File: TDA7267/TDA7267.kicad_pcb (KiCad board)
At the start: 2 copper layers, 43 x 39 mm, 18 parts, among them U1 TDA7267

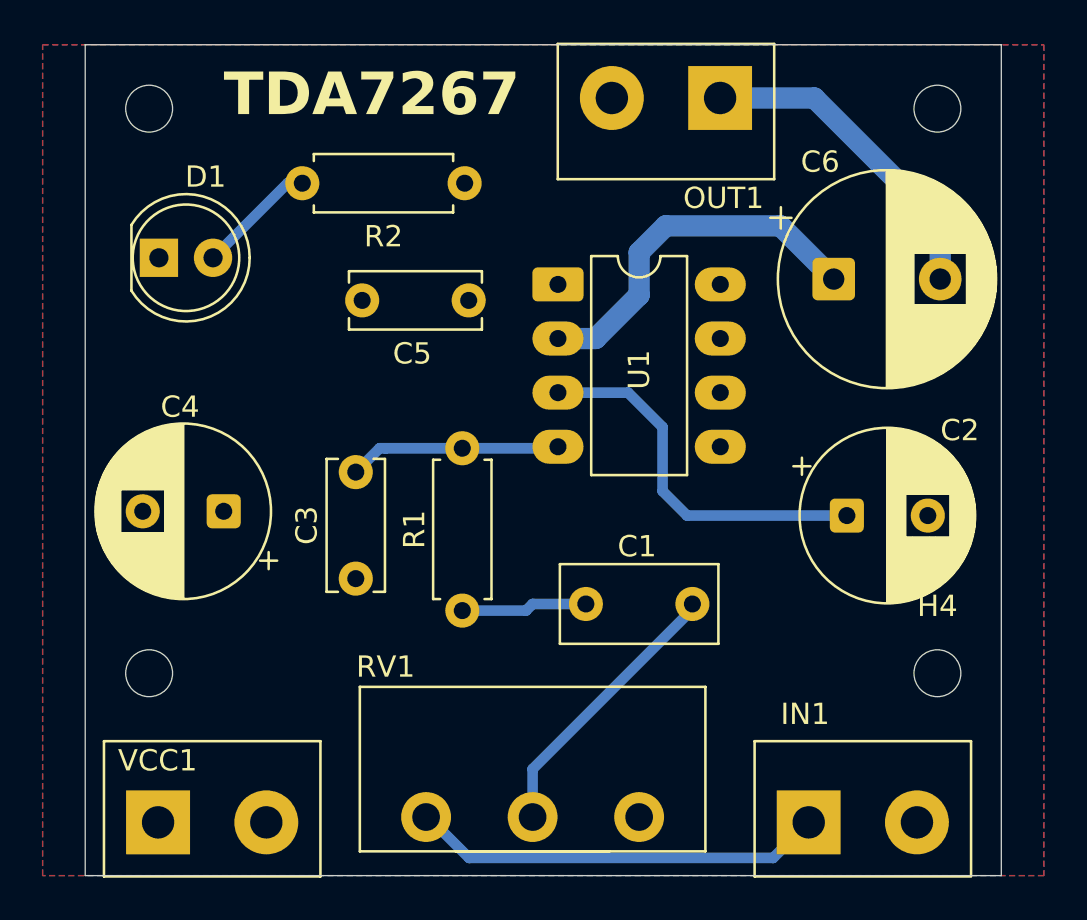
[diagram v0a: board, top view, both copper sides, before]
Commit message: Bottom GND plane
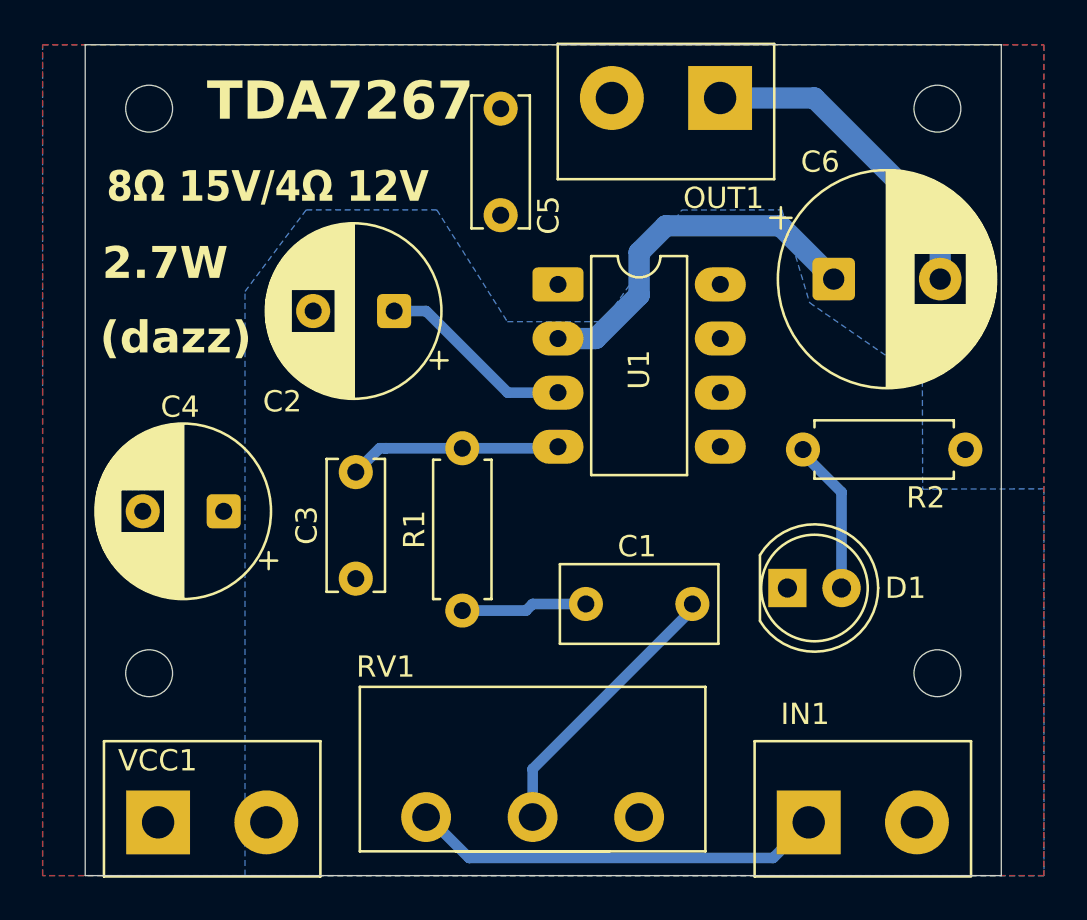
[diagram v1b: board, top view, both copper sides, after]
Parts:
- RV1: value R_Potentiometer -> A10K
- moved D1 33.3 mm to (162.0, 104.0)
- moved R2 26.6 mm to (162.7, 97.5)
- moved C2 23.3 mm to (143.5, 91.0), turned to 180 degrees
- moved C5 11.1 mm to (148.5, 81.5), turned to -90 degrees
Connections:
- net Net-(U1-V+) renamed /VCC
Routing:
- net Net-(U1-SRV): track 17.7 -> 9.28 mm
- net Net-(D1-A): track 5.64 -> 7.25 mm
- added copper zone on B.Cu, net GND
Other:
- board text added: "(dazz)"
- board text added: "2.7W"
- board text added: "8Ω 15V/4Ω 12V"
- board text added: "TDA7267 2.7W Amplifier. 5 to 15V DC supply."
- board text removed: "TDA7267 2W Amplifier. 5 to 15V DC supply."

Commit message: Tweaks
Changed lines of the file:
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@@
 		(hatch edge 0.5)
 		(connect_pads yes
-			(clearance 0.25)
+			(clearance 0.3)
 		)
 		(min_thickness 0.25)
@@
 		(priority 1)
 		(connect_pads yes
-			(clearance 0.5)
+			(clearance 0.3)
 		)
 		(min_thickness 0.25)
@@
 		(polygon
 			(pts
-				(xy 136.5 117.5) (xy 136.5 90.083326) (xy 139.374995 86.25) (xy 145.5 86.25) (xy 148.81579 91.5)
-				(xy 153.342105 91.5) (xy 157 86.259441) (xy 161.7 86.25) (xy 163 90.607672) (xy 168.293873 94.273373)
-				(xy 168.308026 99.362426) (xy 174 99.344523) (xy 174 117.5)
+				(xy 136.5 117.5) (xy 136.5 90.083326) (xy 139.374995 86.25) (xy 145 86.25) (xy 148.31579 91.5) (xy 153.342105 91.5)
+				(xy 157 86.259441) (xy 161.7 86.25) (xy 163 90.607672) (xy 168.293873 94.273373) (xy 168.308026 99.362426)
+				(xy 174 99.344523) (xy 174 117.5)
 			)
 		)
@@
 		(hatch edge 0.5)
 		(connect_pads yes
-			(clearance 0.5)
+			(clearance 0.3)
 		)
 		(min_thickness 0.25)

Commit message: Tweaks
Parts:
- moved C1 1.00 mm to (156.5, 104.8)
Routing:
- net Net-(C1-Pad2): track 5.93 -> 4.93 mm
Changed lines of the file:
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@@
 		(tags "C Disc series Radial pin pitch 5.00mm diameter 6mm width 2.5mm Capacitor")
 		(property "Reference" "C5"
-			(at 5 -2.25 270)
+			(at 4.75 -2.25 270)
 			(layer "F.SilkS")
 			(effects
@@
 	(footprint "Capacitor_THT:C_Rect_L7.2mm_W3.5mm_P5.00mm_FKS2_FKP2_MKS2_MKP2"
 		(layer "F.Cu")
-		(at 157.5 104.75 180)
+		(at 156.5 104.75 180)
 		(descr "C, Rect series, Radial, pin pitch=5.00mm, length*width=7.2*3.5mm^2, Capacitor, http://www.wima.com/EN/WIMA_FKS_2.pdf")
 		(tags "C Rect series Radial pin pitch 5.00mm length 7.2mm width 3.5mm Capacitor")
@@
 		(tags "Resistor Axial_DIN0207 series Axial Horizontal pin pitch 7.62mm 0.25W = 1/4W length 6.3mm diameter 2.5mm")
 		(property "Reference" "R2"
-			(at 5.7621 2.258863 0)
+			(at 3.81 2.25 0)
 			(layer "F.SilkS")
 			(effects
@@
 	)
 	(segment
-		(start 150 104.75)
-		(end 152.5 104.75)
+		(start 146.7 105.06)
+		(end 149.69 105.06)
 		(width 0.5)
 		(layer "B.Cu")
@@
 	)
 	(segment
-		(start 146.7 105.06)
-		(end 149.69 105.06)
+		(start 150 104.75)
+		(end 151.5 104.75)
 		(width 0.5)
 		(layer "B.Cu")
@@
 	)
 	(segment
-		(start 157.5 105)
-		(end 150 112.5)
+		(start 150 114.75)
+		(end 150 113)
 		(width 0.5)
 		(layer "B.Cu")
@@
 	)
 	(segment
-		(start 150 112.5)
-		(end 150 114.75)
+		(start 150 113)
+		(end 156.5 106.5)
 		(width 0.5)
 		(layer "B.Cu")
@@
 	)
 	(segment
-		(start 157.5 104.75)
-		(end 157.5 105)
+		(start 156.5 106.5)
+		(end 156.5 104.75)
 		(width 0.5)
 		(layer "B.Cu")
